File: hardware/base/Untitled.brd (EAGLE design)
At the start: 83.2 x 83.2 mm, 30 parts, among them Q1 IRLML2502, Q2 IRLML2502, Q3 IRLML2502, Q4 IRLML2502, U2 MIC5205

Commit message: 20160415
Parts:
- removed C9: 0.1uF, SparkFun-Capacitors:0402-CAP
- removed U$2: ESP07, esp8266modules:ESP07
- added U$3: ESP12, esp8266modules:ESP12
- moved R1 45.2 mm to (29.2, 31.8), turned to 90 degrees
- moved POWER 28.1 mm to (25.4, 53.3), turned to 45 degrees
- moved C2 27.1 mm to (37.5, 52.7), turned to 180 degrees
- moved FTDI 25.4 mm to (40.6, 27.9)
- moved C1 22.2 mm to (33.0, 50.8), turned to 90 degrees
- moved U2 17.4 mm to (37.5, 49.5), turned to 90 degrees
- moved C10 11.0 mm to (41.3, 33.0), turned to 90 degrees
- moved C6 9.09 mm to (43.8, 33.0), turned to 90 degrees
- moved C14 8.08 mm to (46.4, 33.0), turned to 90 degrees
- moved R4 3.24 mm to (38.7, 33.0), turned to 270 degrees
- moved R5 2.01 mm to (36.2, 33.0), turned to 90 degrees
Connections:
- removed net 5V: C9.1
- removed net N$21: R1.2, U$2.GPIO15
- new net N$20: R1.2, U$3.GPIO15
- net 3.3V: now also U$3.CH_PD, U$3.GPIO2, U$3.VCC; no longer U$2.CH_PD, U$2.GPIO2, U$2.VCC
- net DTR: now also U$3.GPIO0; no longer U$2.GPIO0
- net GND: now also U$3.GND; no longer C9.2, U$2.GND
- net M1: now also U$3.GPIO14; no longer U$2.GPIO14
- net M2: now also U$3.GPIO12; no longer U$2.GPIO12
- net M3: now also U$3.GPIO13; no longer U$2.GPIO13
- net M4: now also U$3.GPIO16; no longer U$2.GPIO16
- net RX: now also U$3.RX; no longer U$2.RX
- net SCL: now also U$3.GPIO4
- net SDA: now also U$3.GPIO5
- net TX: now also U$3.TX; no longer U$2.TX
- net VCC: now also U$3.ADC

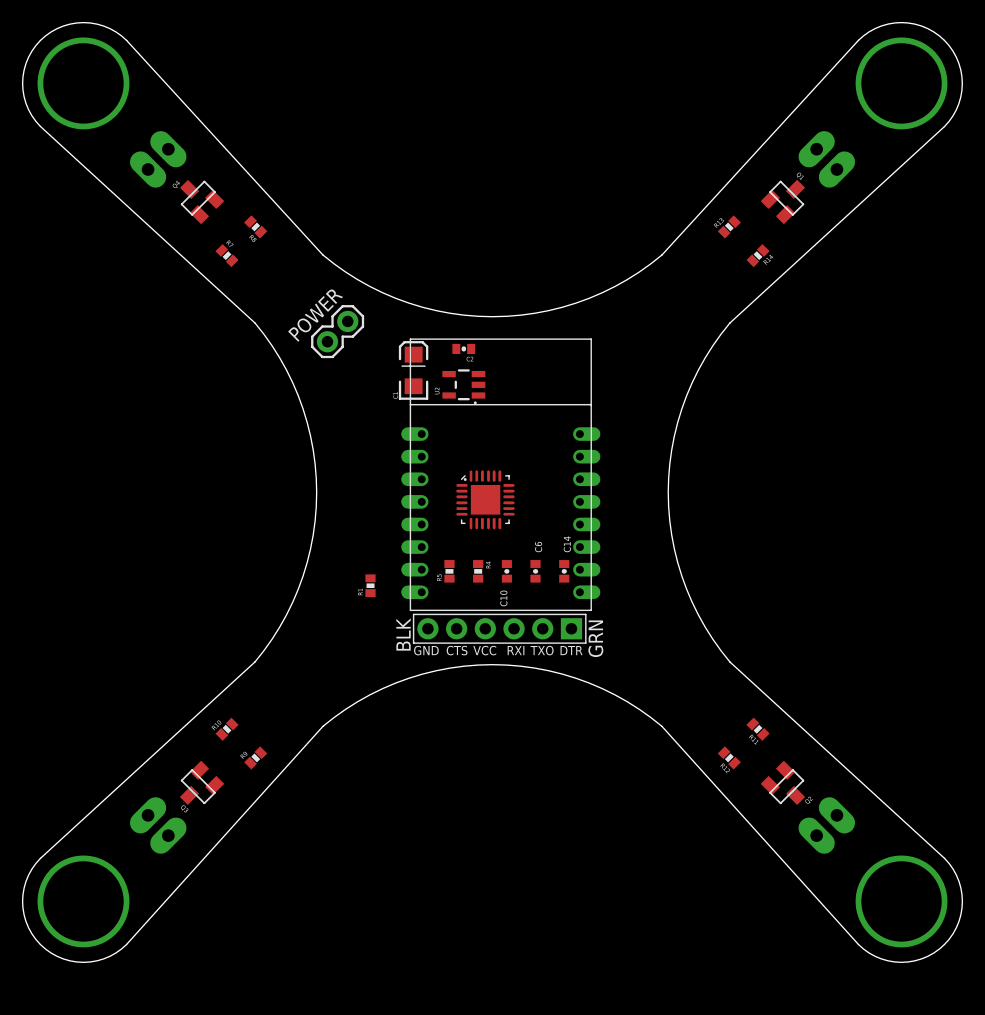
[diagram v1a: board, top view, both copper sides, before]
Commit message: add switch
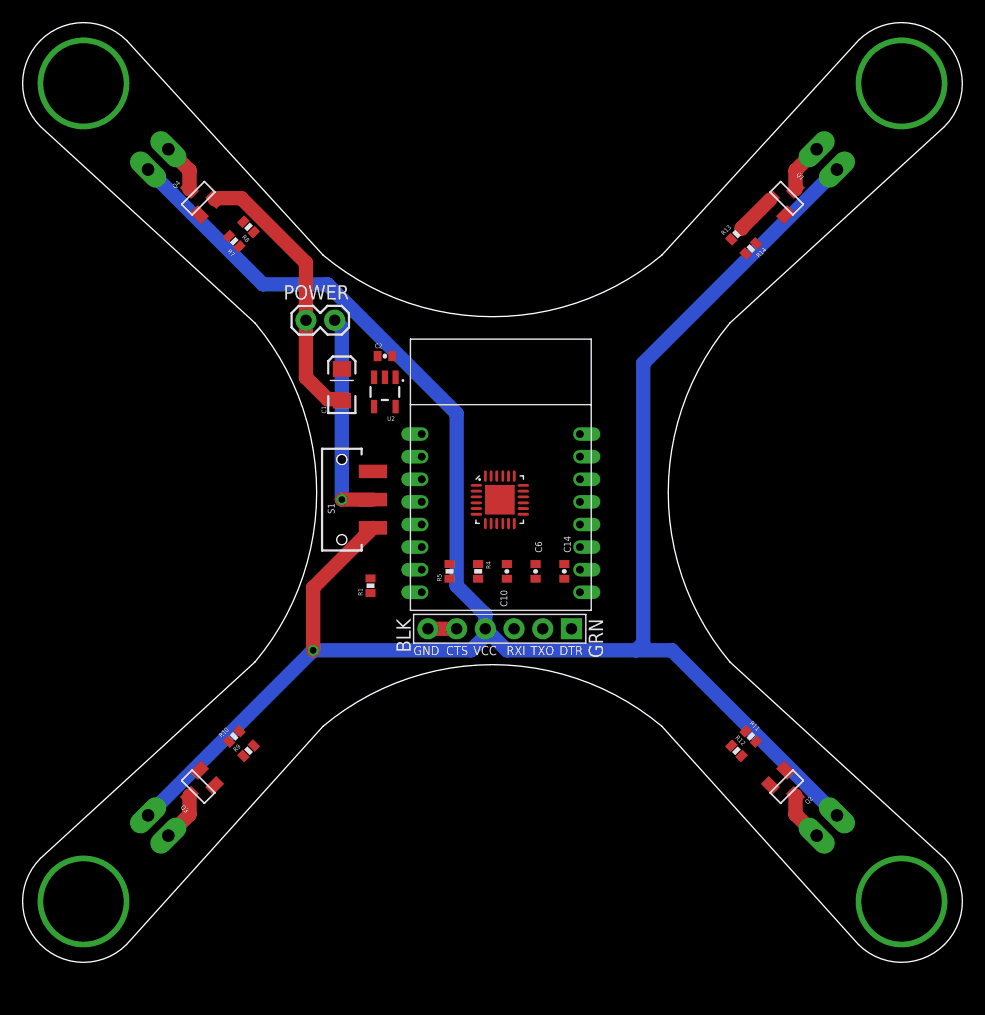
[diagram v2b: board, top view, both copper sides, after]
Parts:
- added S1: (no value), SparkFun-Electromechanical:SWITCH-SPDT-SMD
- moved C2 7.01 mm to (30.5, 52.1), turned to 0 degrees
- moved U2 7.01 mm to (30.5, 48.9), turned to 180 degrees
- moved C1 6.48 mm to (26.7, 49.5)
- moved POWER 2.69 mm to (23.5, 55.2), turned to 0 degrees
- moved R7 1.42 mm to (17.1, 62.2), turned to 135 degrees
- moved U$1 1.27 mm to (40.6, 39.4)
- moved R10 0.90 mm to (17.1, 18.4)
- moved R11 0.90 mm to (62.9, 18.4), turned to 315 degrees
- moved R9 0.90 mm to (18.4, 17.1)
- moved R12 0.90 mm to (61.6, 17.1), turned to 315 degrees
- moved R13 0.90 mm to (61.6, 62.9)
- moved R14 0.90 mm to (62.9, 61.6)
- moved R8 0.64 mm to (18.4, 63.5)
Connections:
- new net N$6: POWER.2, S1.2
- net VCC: now also S1.1; no longer POWER.2
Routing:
- net VCC: track 0.00 -> 194.3 mm, vias 0 -> 1
- net GND: track 0.00 -> 27.2 mm
- net N$6: track 0.00 -> 18.9 mm, vias 0 -> 1
- net N$3: track 0.00 -> 4.33 mm
- net N$14: track 0.00 -> 4.33 mm
- net N$8: track 0.00 -> 4.33 mm
- net N$12: track 0.00 -> 4.33 mm
- net N$41: track 0.00 -> 3.66 mm
